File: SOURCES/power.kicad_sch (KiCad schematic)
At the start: 22 parts, among them P13 CONN_01X02, P20 TST, U7 LM2842Y

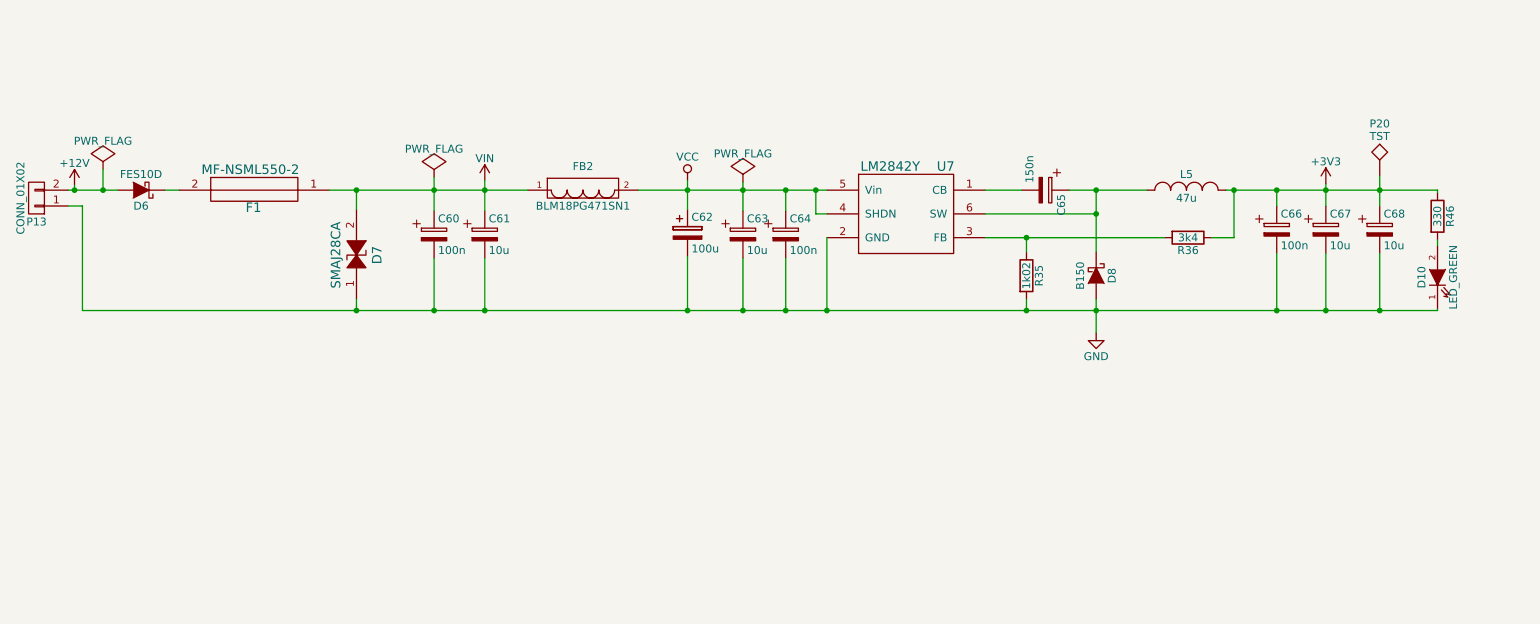
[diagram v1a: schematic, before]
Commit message: Removed redundant 7414 and pot, rerouted a bit.
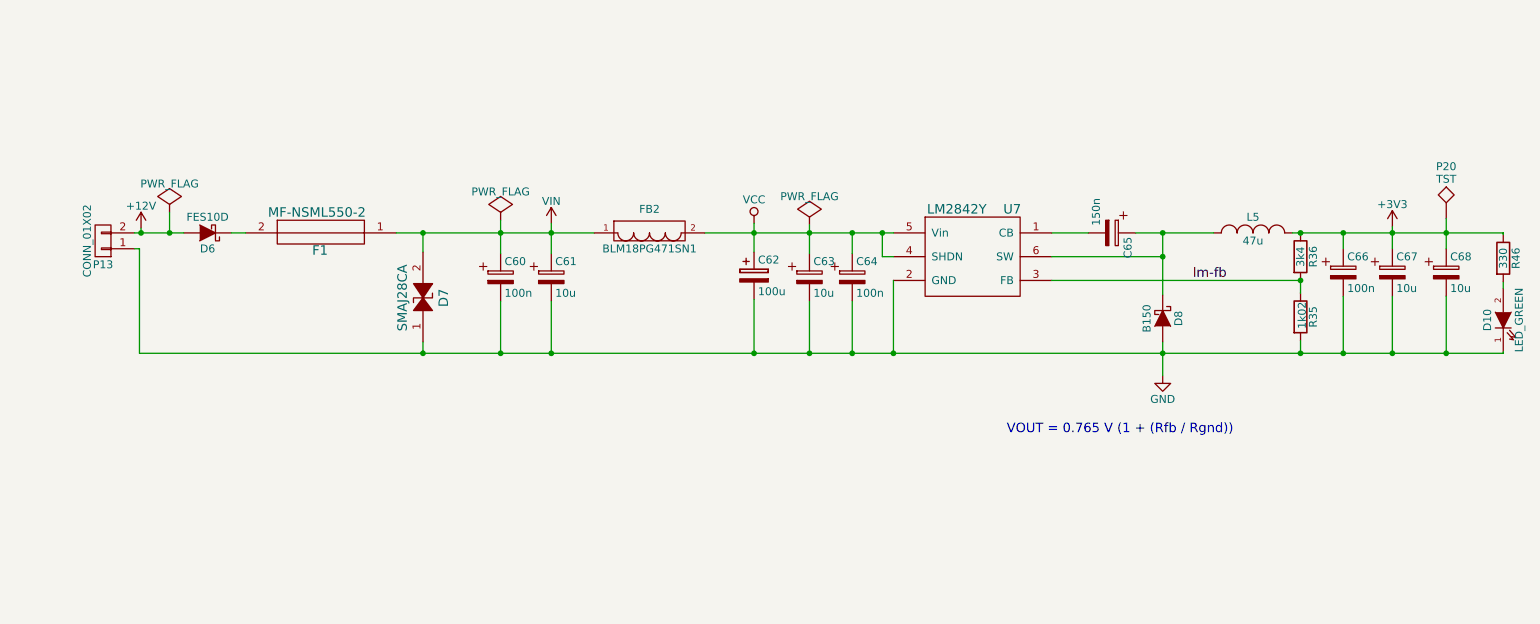
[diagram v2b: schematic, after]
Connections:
- net lm-fb: now reaches R35.1, R36.2, U7.3 (FB)
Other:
- note added: "VOUT = 0.765 V (1 + (Rfb / Rgnd))"
- moved on the sheet: C60, C61, C62, C63, C64, C65, C66, C67, C68, D10, D6, D7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

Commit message: Removed ArduinoPort, Changed Power Supply. Rerouting and stuff.
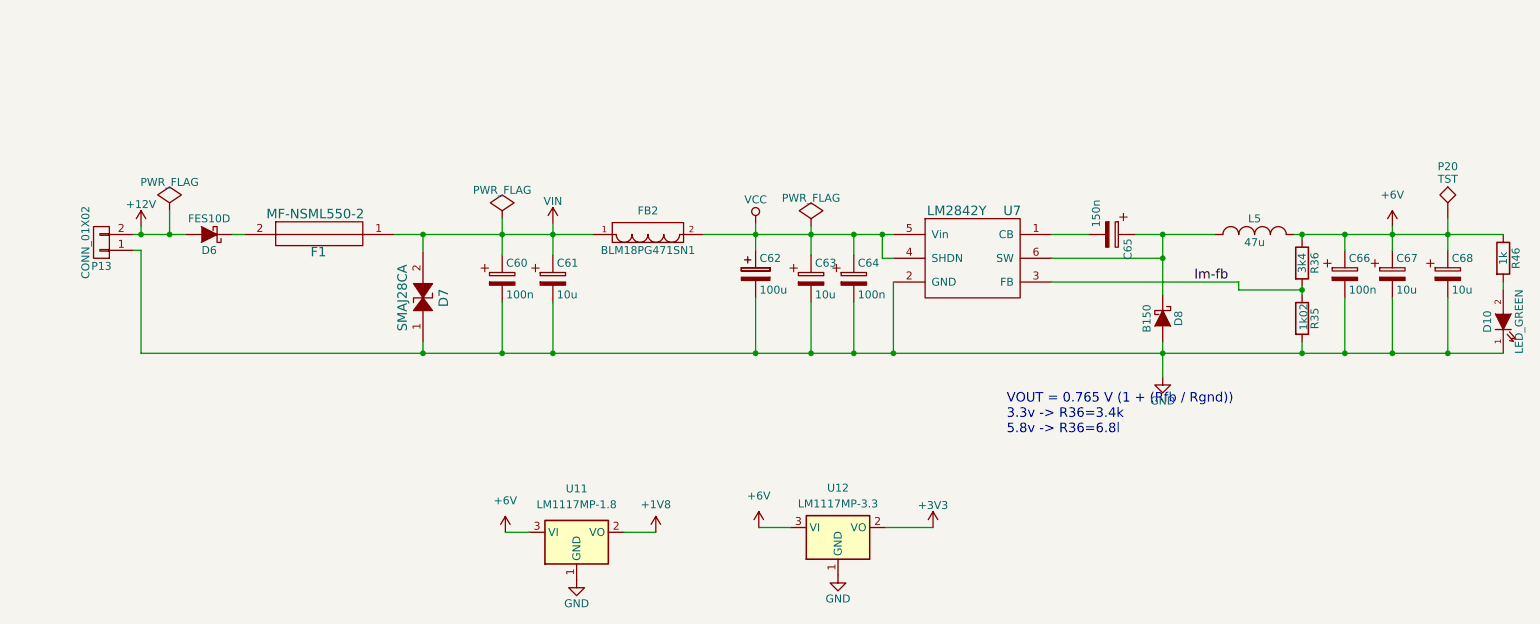
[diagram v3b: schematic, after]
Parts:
- added U11: LM1117MP-1.8, Package_TO_SOT_SMD:SOT-223-3_TabPin2, symbol Regulator_Linear:LM1117MP-1.8
- added U12: LM1117MP-3.3, Package_TO_SOT_SMD:SOT-223-3_TabPin2, symbol Regulator_Linear:LM1117MP-3.3
- R46: value 330 -> 1k
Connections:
- net +3V3: now also U12.2 (VO); no longer C66.1, C67.1, C68.1, L5.2, P20.1, R36.1, R46.1
- net GND: now also U11.1 (GND), U12.1 (GND)
- new net +1V8: U11.2 (VO)
- new net +6V: C66.1, C67.1, C68.1, L5.2, P20.1, R36.1, R46.1, U11.3 (VI), U12.3 (VI)
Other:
- note added: "VOUT = 0.765 V (1 + (Rfb / Rgnd)) 3.3v -> R36=3.4k 5.8v -> R36=6.8l"
- note removed: "VOUT = 0.765 V (1 + (Rfb / Rgnd))"
- moved on the sheet: R36

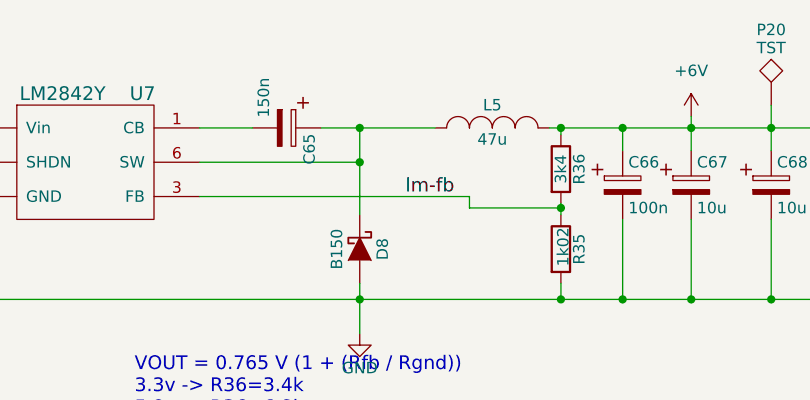
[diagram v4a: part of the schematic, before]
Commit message: Optimized Vreg traces.
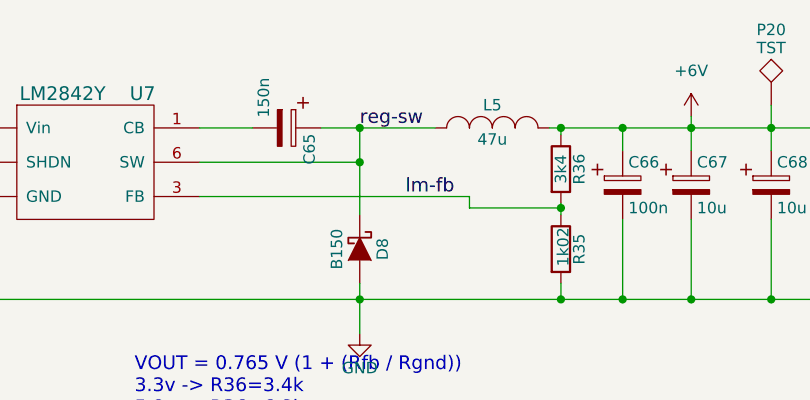
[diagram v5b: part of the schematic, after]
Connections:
- net reg-sw: now reaches C65.1, D8.1 (K), L5.1, U7.6 (SW)
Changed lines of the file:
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@@
+    (effects (font (size 1.524 1.524)) (justify left bottom))
+  )
+  (label "reg-sw" (at 200.66 85.09 0) (fields_autoplaced)
     (effects (font (size 1.524 1.524)) (justify left bottom))
   )

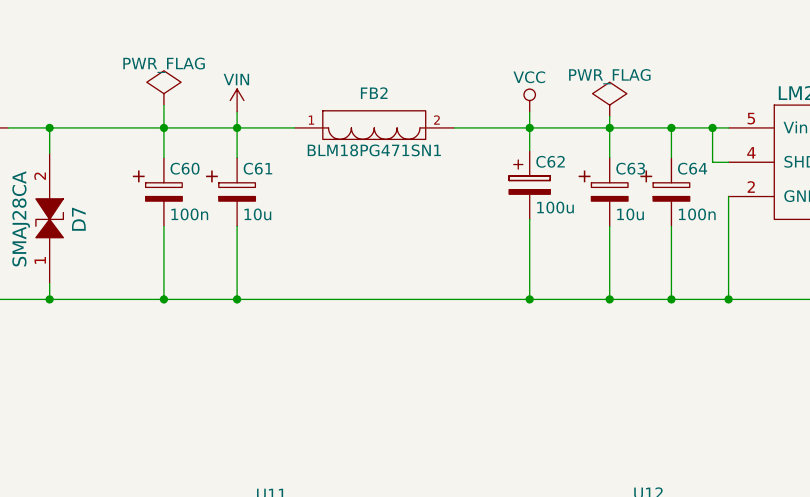
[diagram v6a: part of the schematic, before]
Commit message: Fixed Vin/Vcc issue.
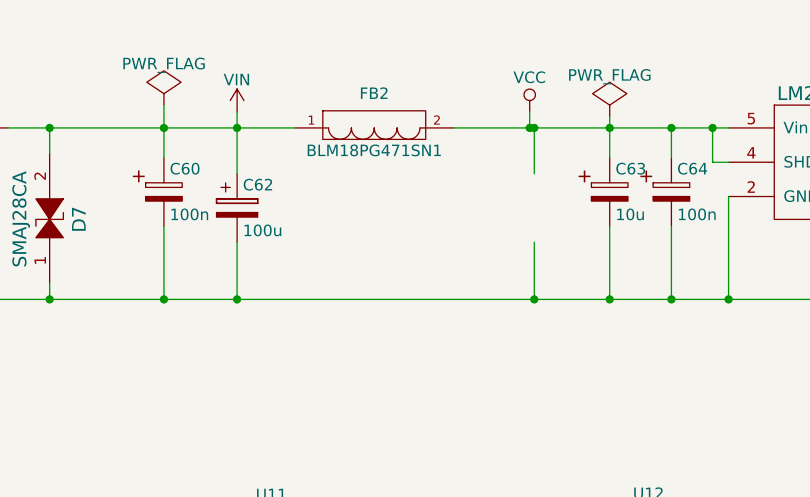
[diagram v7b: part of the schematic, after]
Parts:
- removed C61: 10u, fdsp_capacitor:C_1206_HandSoldering, symbol MyLibrary:C
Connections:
- net VCC: no longer C62.1
- net VIN: now also C62.1
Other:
- moved on the sheet: C62

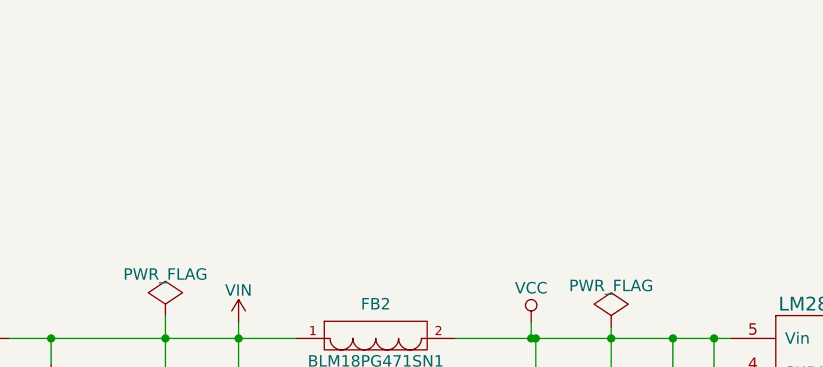
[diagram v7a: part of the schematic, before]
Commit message: Improved power traces.
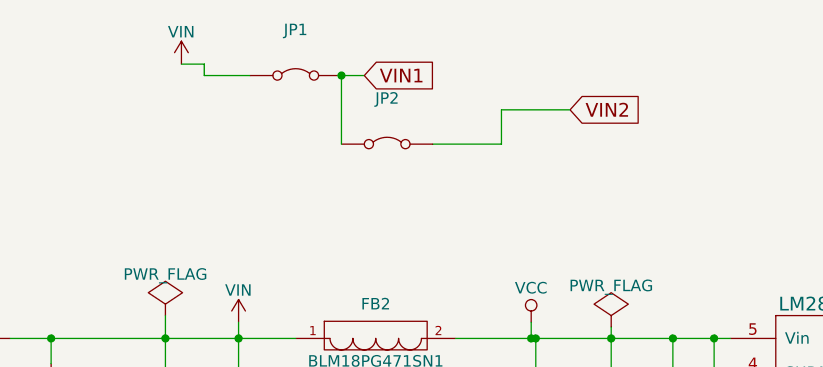
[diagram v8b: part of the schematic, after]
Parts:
- added JP1, JP2: Jumper_2_Bridged, JumperWires:Jumper-Wire_25mm_Blue, symbol Jumper:Jumper_2_Bridged
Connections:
- net VIN: now also JP1.1 (A)
- new net VIN1: JP1.2 (B), JP2.1 (A)
- new net VIN2: JP2.2 (B)
